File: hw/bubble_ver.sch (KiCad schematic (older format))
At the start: 0 parts

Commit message: - add ic (freescale mkl02), temp sensor (silabs si7020), bubble display (hp qdsp-6040) to schematic
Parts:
- added D?: QDSP-6040, symbol QDSP-6040
- added U?: MKL02ZXVFG4, ~, symbol MKL02ZXVFG4
- added U?: SI7020, ~, symbol SI7020
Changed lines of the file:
@@
 LIBS:contrib
 LIBS:valves
+LIBS:kicadlib
+LIBS:bubble_ver-cache
 EELAYER 27 0
 EELAYER END
@@
 Comment4 ""
 $EndDescr
+$Comp
+L MKL02ZXVFG4 U?
+U 1 1 539905F5
+P 4500 3000
+F 0 "U?" H 4050 2400 60  0000 C CNN
+F 1 "MKL02ZXVFG4" H 5200 2400 60  0000 C CNN
+F 2 "~" H 4500 3000 60  0000 C CNN
+F 3 "~" H 4500 3000 60  0000 C CNN
+	1    4500 3000
+	1    0    0    -1
+$EndComp
+$Comp
+L SI7020 U?
+U 1 1 53990604
+P 6250 4500
+F 0 "U?" H 6250 4200 60  0000 C CNN
+F 1 "SI7020" H 6250 4800 60  0000 C CNN
+F 2 "~" H 6250 4400 60  0000 C CNN
+F 3 "~" H 6250 4400 60  0000 C CNN
+	1    6250 4500
+	1    0    0    -1
+$EndComp
+$Comp
+L QDSP-6040 D?
+U 1 1 5399119B
+P 7700 3900
+F 0 "D?" H 8600 4650 60  0000 C CNN
+F 1 "QDSP-6040" V 7550 4650 60  0000 C CNN
+F 2 "" H 8500 4400 60  0000 C CNN
+F 3 "" H 8500 4400 60  0000 C CNN
+	1    7700 3900
+	1    0    0    -1
+$EndComp
 $EndSCHEMATC

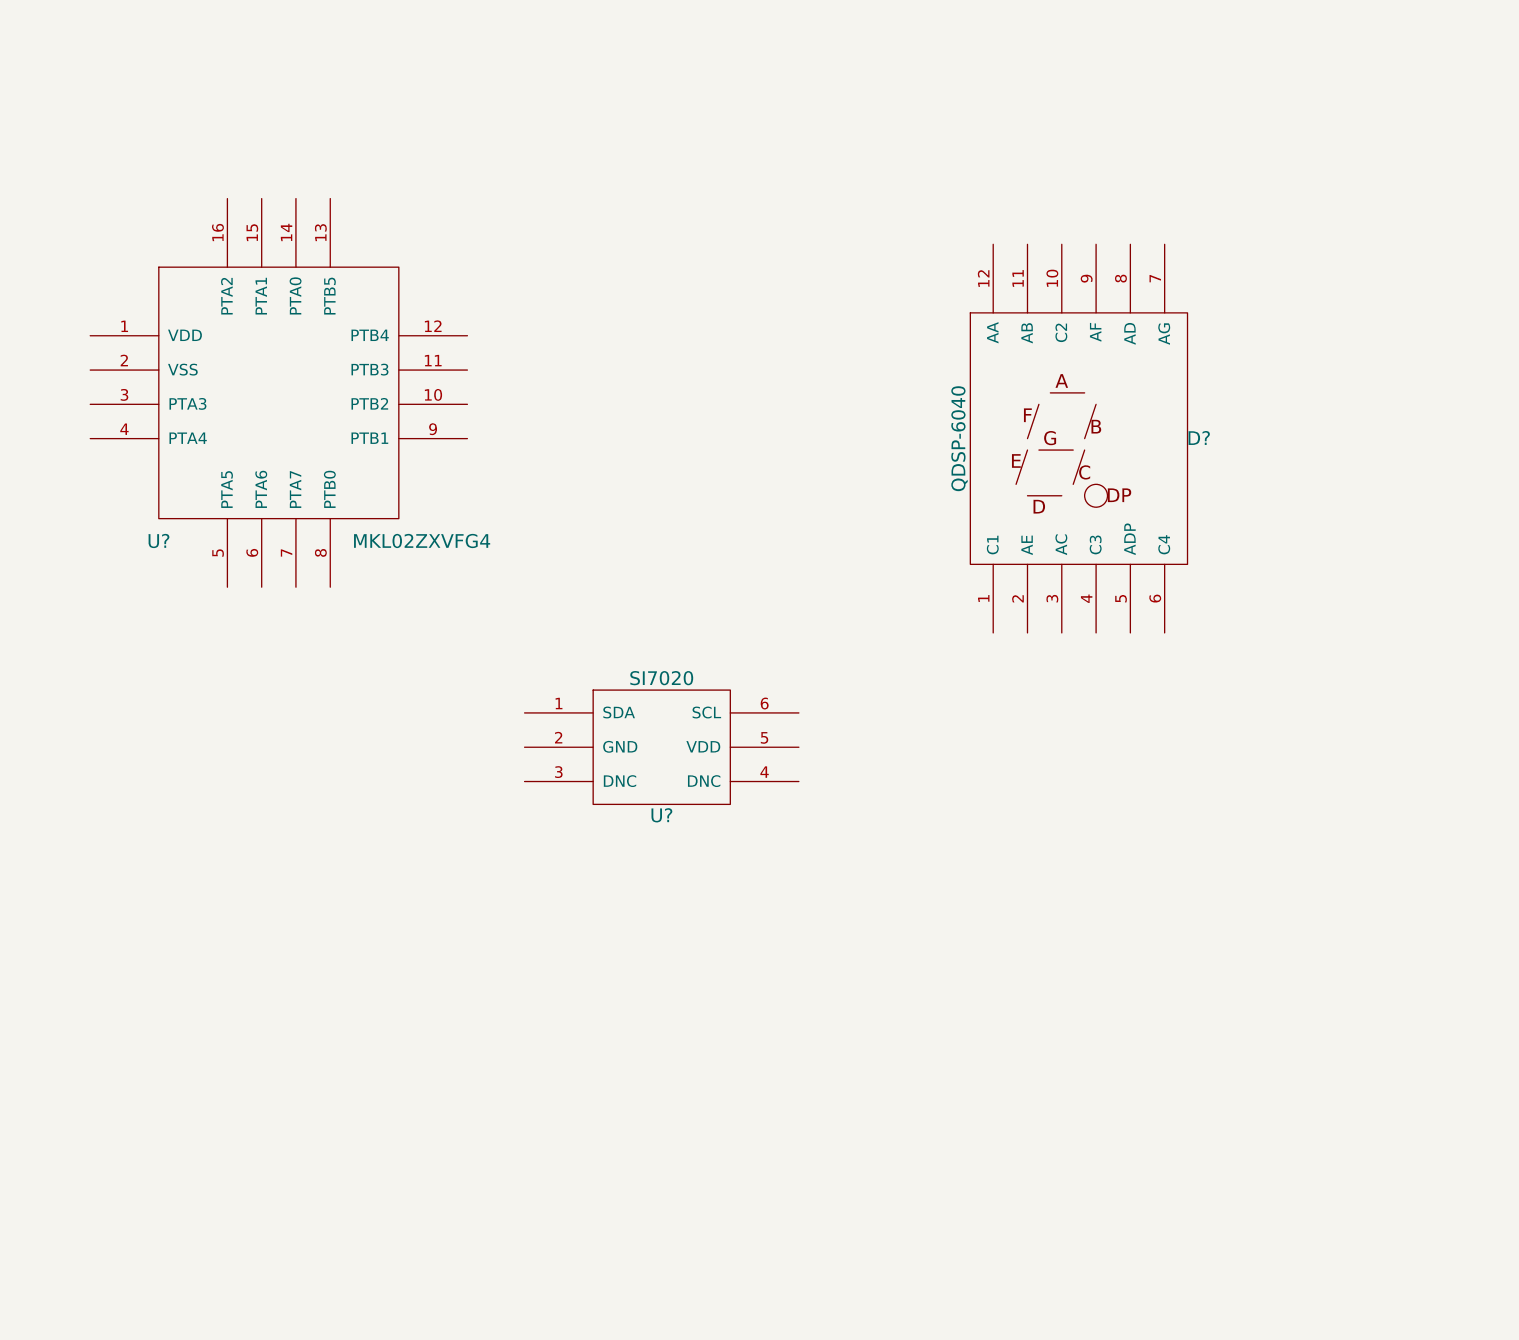
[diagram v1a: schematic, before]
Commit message: - start flushing out schematic. use dual-io multiplexing for leds (better than charlieplexing, no leak, and I have enough MCU pins)
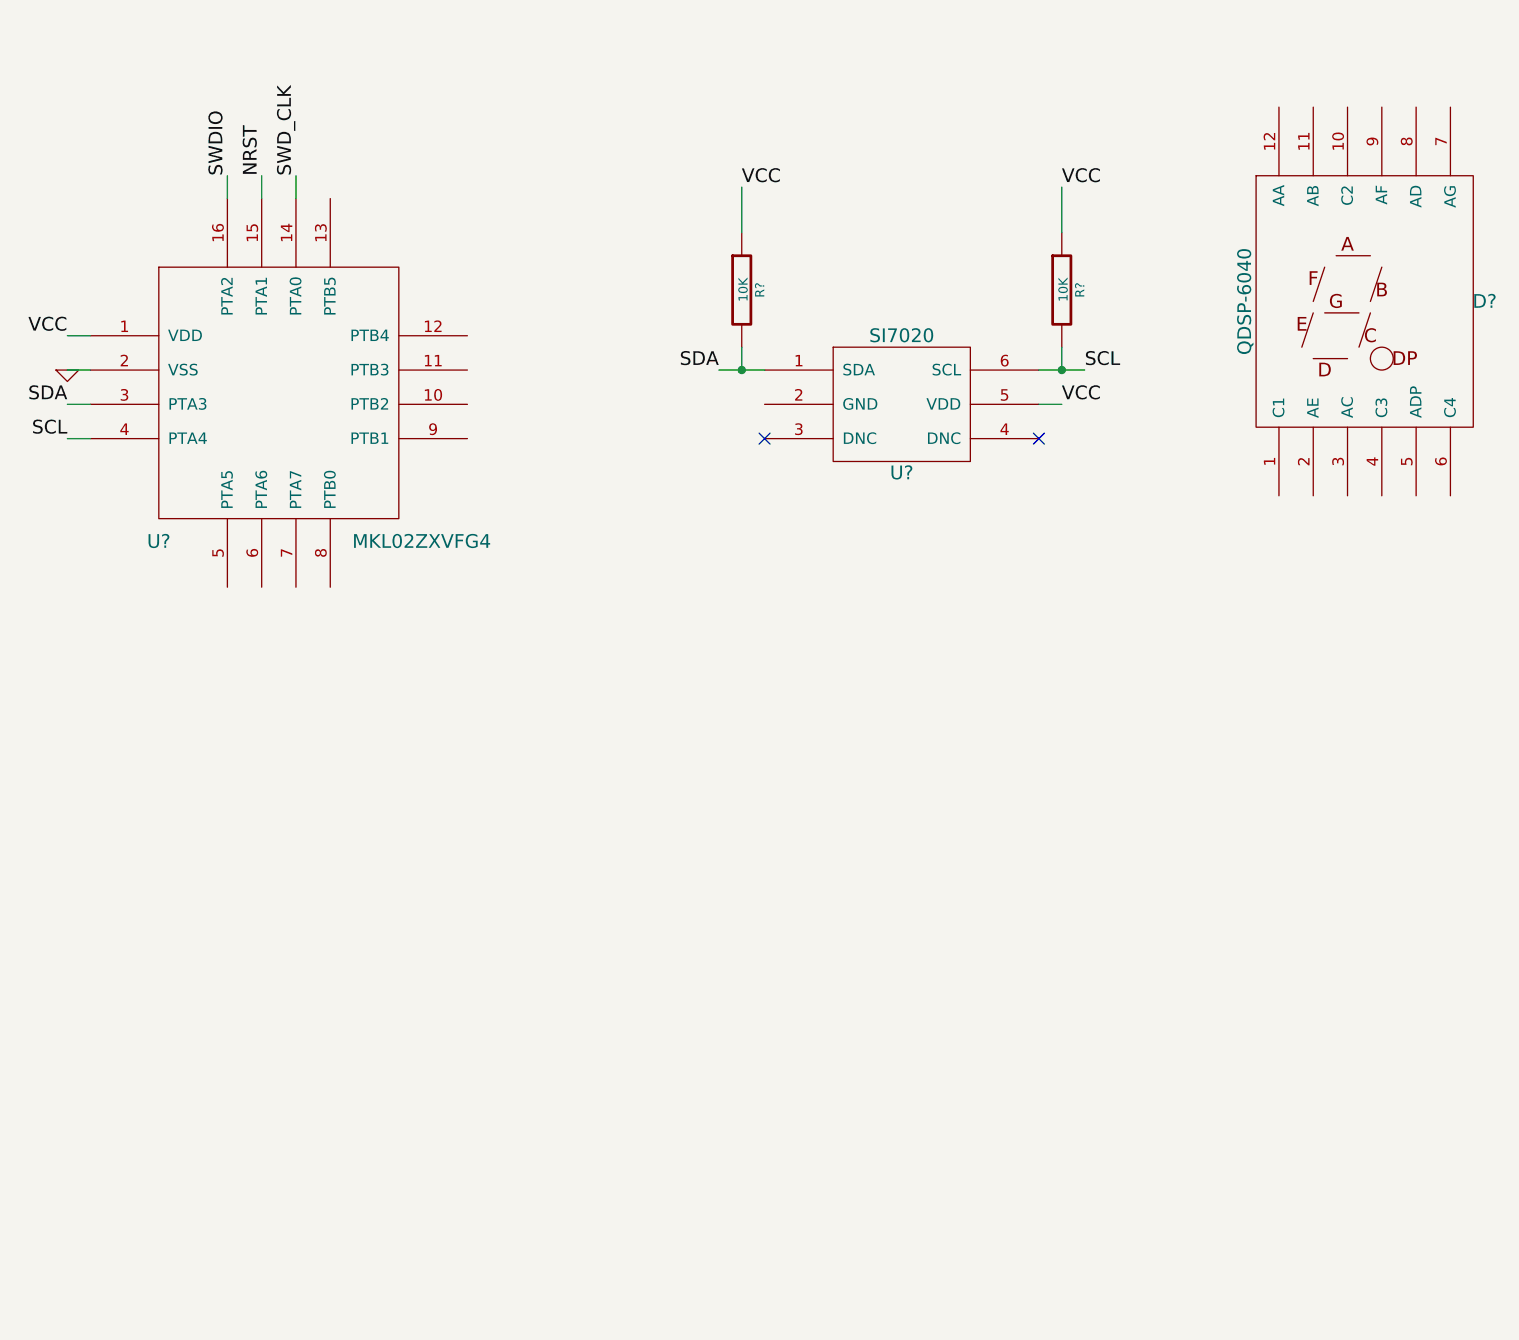
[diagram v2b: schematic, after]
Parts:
- added R? (x2): 10K, ~, symbol R
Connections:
- net VCC: now reaches U?.1 (VDD)
- net VCC: now also U?.5 (VDD), R?.1, R?.1
- net SWD_CLK: now reaches U?.14 (PTA0)
- net NRST: now reaches U?.15 (PTA1)
- net SWDIO: now reaches U?.16 (PTA2)
- net GND: now reaches U?.2 (VSS)
- net SDA: now reaches U?.3 (PTA3)
- net SDA: now also U?.1 (SDA), R?.2
- net SCL: now reaches U?.4 (PTA4)
- net SCL: now also U?.6 (SCL), R?.2
- no-connect marks 0 -> 2
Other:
- moved on the sheet: D?, U?
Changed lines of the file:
@@
 L SI7020 U?
 U 1 1 53990604
-P 6250 4500
-F 0 "U?" H 6250 4200 60  0000 C CNN
-F 1 "SI7020" H 6250 4800 60  0000 C CNN
-F 2 "~" H 6250 4400 60  0000 C CNN
-F 3 "~" H 6250 4400 60  0000 C CNN
-	1    6250 4500
+P 7300 3000
+F 0 "U?" H 7300 2700 60  0000 C CNN
+F 1 "SI7020" H 7300 3300 60  0000 C CNN
+F 2 "~" H 7300 2900 60  0000 C CNN
+F 3 "~" H 7300 2900 60  0000 C CNN
+	1    7300 3000
 	1    0    0    -1
 $EndComp
@@
 L QDSP-6040 D?
 U 1 1 5399119B
-P 7700 3900
-F 0 "D?" H 8600 4650 60  0000 C CNN
-F 1 "QDSP-6040" V 7550 4650 60  0000 C CNN
-F 2 "" H 8500 4400 60  0000 C CNN
-F 3 "" H 8500 4400 60  0000 C CNN
-	1    7700 3900
+P 8950 3300
+F 0 "D?" H 9850 4050 60  0000 C CNN
+F 1 "QDSP-6040" V 8800 4050 60  0000 C CNN
+F 2 "" H 9750 3800 60  0000 C CNN
+F 3 "" H 9750 3800 60  0000 C CNN
+	1    8950 3300
 	1    0    0    -1
 $EndComp
+$Comp
+L R R?
+U 1 1 5399E115
+P 6600 2500
+F 0 "R?" V 6680 2500 40  0000 C CNN
+F 1 "10K" V 6607 2501 40  0000 C CNN
+F 2 "~" V 6530 2500 30  0000 C CNN
+F 3 "~" H 6600 2500 30  0000 C CNN
+	1    6600 2500
+	1    0    0    -1
+$EndComp
+$Comp
+L R R?
+U 1 1 5399E127
+P 8000 2500
+F 0 "R?" V 8080 2500 40  0000 C CNN
+F 1 "10K" V 8007 2501 40  0000 C CNN
+F 2 "~" V 7930 2500 30  0000 C CNN
+F 3 "~" H 8000 2500 30  0000 C CNN
+	1    8000 2500
+	1    0    0    -1
+$EndComp
+Wire Wire Line
+	6600 2250 6600 2050
+Wire Wire Line
+	8000 2250 8000 2050
+Text Label 8000 2050 0    60   ~ 0
+VCC
+Text Label 6600 2050 0    60   ~ 0
+VCC
+Wire Wire Line
+	8000 2750 8000 2850
+Wire Wire Line
+	7900 2850 8100 2850
+Wire Wire Line
+	6500 2850 6700 2850
+Wire Wire Line
+	6600 2850 6600 2750
+NoConn ~ 7900 3150
+NoConn ~ 6700 3150
+Connection ~ 8000 2850
+Connection ~ 6600 2850
+Text Label 8100 2850 0    60   ~ 0
+SCL
+Text Label 6500 2850 2    60   ~ 0
+SDA
+Text Label 3650 3000 2    60   ~ 0
+SDA
+Text Label 3650 3150 2    60   ~ 0
+SCL
+Wire Wire Line
+	3750 3000 3650 3000
+Wire Wire Line
+	3650 3150 3750 3150
+Text Label 3650 2700 2    60   ~ 0
+VCC
+Wire Wire Line
+	3650 2700 3750 2700
+$Comp
+L GND #PWR?
+U 1 1 5399E2DF
+P 3650 2850
+F 0 "#PWR?" H 3650 2850 30  0001 C CNN
+F 1 "GND" H 3650 2780 30  0001 C CNN
+F 2 "" H 3650 2850 60  0000 C CNN
+F 3 "" H 3650 2850 60  0000 C CNN
+	1    3650 2850
+	1    0    0    -1
+$EndComp
+Wire Wire Line
+	3650 2850 3750 2850
+Text Label 4350 2000 1    60   ~ 0
+SWDIO
+Text Label 4500 2000 1    60   ~ 0
+NRST
+Text Label 4650 2000 1    60   ~ 0
+SWD_CLK
+Wire Wire Line
+	4350 2000 4350 2100
+Wire Wire Line
+	4500 2000 4500 2100
+Wire Wire Line
+	4650 2000 4650 2100
+Text Label 8000 3000 0    60   ~ 0
+VCC
+Wire Wire Line
+	8000 3000 7900 3000
 $EndSCHEMATC

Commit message: - add resistor networks and most net names.
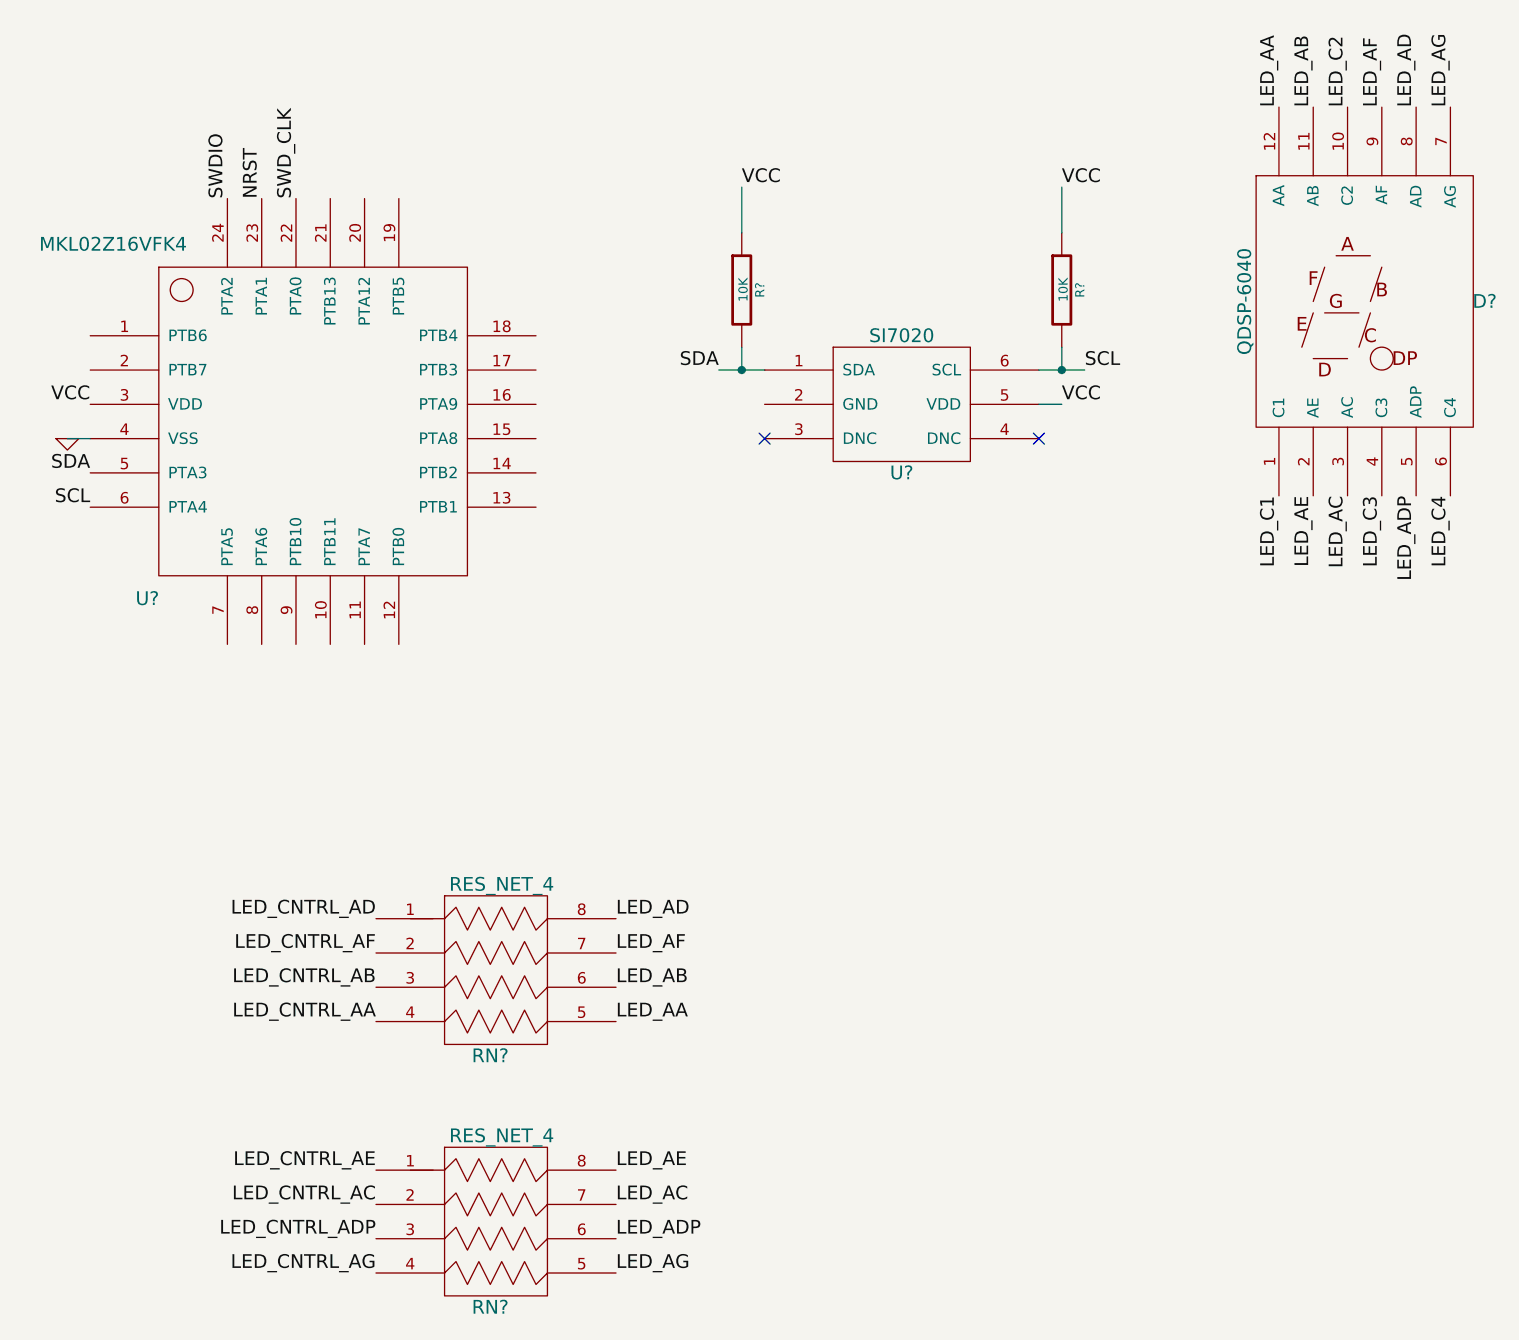
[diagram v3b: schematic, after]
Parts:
- removed U?: MKL02ZXVFG4, ~, symbol MKL02ZXVFG4
- added RN? (x2): RES_NET_4, symbol RES_NET_4
- added U?: MKL02Z16VFK4, symbol MKL02Z16VFK4
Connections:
- net GND: now also U?.4 (VSS)
- net NRST: now also U?.23 (PTA1)
- net SCL: now also U?.6 (PTA4)
- net SDA: now also U?.5 (PTA3)
- net SWDIO: now also U?.24 (PTA2)
- net SWD_CLK: now also U?.22 (PTA0)
- net VCC: now also U?.3 (VDD)
- net LED_C1: now reaches D?.1 (C1)
- net LED_C2: now reaches D?.10 (C2)
- net LED_AB: now reaches D?.11 (AB)
- net LED_AB: now also RN?.6
- net LED_AA: now reaches D?.12 (AA)
- net LED_AA: now also RN?.5
- net LED_AE: now reaches D?.2 (AE)
- net LED_AE: now also RN?.8
- net LED_AC: now reaches D?.3 (AC)
- net LED_AC: now also RN?.7
- net LED_C3: now reaches D?.4 (C3)
- net LED_ADP: now reaches D?.5 (ADP)
- net LED_ADP: now also RN?.6
- net LED_C4: now reaches D?.6 (C4)
- net LED_AG: now reaches D?.7 (AG)
- net LED_AG: now also RN?.5
- net LED_AD: now reaches D?.8 (AD)
- net LED_AD: now also RN?.8
- net LED_AF: now reaches D?.9 (AF)
- net LED_AF: now also RN?.7
- new net LED_CNTRL_AA: RN?.4
- new net LED_CNTRL_AB: RN?.3
- new net LED_CNTRL_AC: RN?.2
- new net LED_CNTRL_AD: RN?.1
- new net LED_CNTRL_ADP: RN?.3
- new net LED_CNTRL_AE: RN?.1
- new net LED_CNTRL_AF: RN?.2
- new net LED_CNTRL_AG: RN?.4
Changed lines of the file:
@@
 $EndDescr
-$Comp
-L MKL02ZXVFG4 U?
-U 1 1 539905F5
-P 4500 3000
-F 0 "U?" H 4050 2400 60  0000 C CNN
-F 1 "MKL02ZXVFG4" H 5200 2400 60  0000 C CNN
-F 2 "~" H 4500 3000 60  0000 C CNN
-F 3 "~" H 4500 3000 60  0000 C CNN
-	1    4500 3000
-	1    0    0    -1
-$EndComp
 $Comp
 L SI7020 U?
@@
 Text Label 6500 2850 2    60   ~ 0
 SDA
-Text Label 3650 3000 2    60   ~ 0
+Text Label 3750 3300 2    60   ~ 0
 SDA
-Text Label 3650 3150 2    60   ~ 0
+Text Label 3750 3450 2    60   ~ 0
 SCL
-Wire Wire Line
-	3750 3000 3650 3000
-Wire Wire Line
-	3650 3150 3750 3150
-Text Label 3650 2700 2    60   ~ 0
+Text Label 3750 3000 2    60   ~ 0
 VCC
-Wire Wire Line
-	3650 2700 3750 2700
 $Comp
 L GND #PWR?
 U 1 1 5399E2DF
-P 3650 2850
-F 0 "#PWR?" H 3650 2850 30  0001 C CNN
-F 1 "GND" H 3650 2780 30  0001 C CNN
-F 2 "" H 3650 2850 60  0000 C CNN
-F 3 "" H 3650 2850 60  0000 C CNN
-	1    3650 2850
+P 3650 3150
+F 0 "#PWR?" H 3650 3150 30  0001 C CNN
+F 1 "GND" H 3650 3080 30  0001 C CNN
+F 2 "" H 3650 3150 60  0000 C CNN
+F 3 "" H 3650 3150 60  0000 C CNN
+	1    3650 3150
 	1    0    0    -1
 $EndComp
 Wire Wire Line
-	3650 2850 3750 2850
-Text Label 4350 2000 1    60   ~ 0
+	3650 3150 3750 3150
+Text Label 4350 2100 1    60   ~ 0
 SWDIO
-Text Label 4500 2000 1    60   ~ 0
+Text Label 4500 2100 1    60   ~ 0
 NRST
-Text Label 4650 2000 1    60   ~ 0
+Text Label 4650 2100 1    60   ~ 0
 SWD_CLK
-Wire Wire Line
-	4350 2000 4350 2100
-Wire Wire Line
-	4500 2000 4500 2100
-Wire Wire Line
-	4650 2000 4650 2100
 Text Label 8000 3000 0    60   ~ 0
 VCC
 Wire Wire Line
 	8000 3000 7900 3000
+Text Label 8950 1700 1    60   ~ 0
+LED_AA
+Text Label 9100 1700 1    60   ~ 0
+LED_AB
+Text Label 9100 3400 3    60   ~ 0
+LED_AE
+Text Label 9250 3400 3    60   ~ 0
+LED_AC
+$Comp
+L MKL02Z16VFK4 U?
+U 1 1 5399EECC
+P 4500 3150
+F 0 "U?" H 4000 2450 60  0000 C CNN
+F 1 "MKL02Z16VFK4" H 3850 4000 60  0000 C CNN
+F 2 "" H 4500 3150 60  0000 C CNN
+F 3 "" H 4500 3150 60  0000 C CNN
+	1    4500 3150
+	1    0    0    -1
+$EndComp
+Text Label 9250 1700 1    60   ~ 0
+LED_C2
+Text Label 9400 1700 1    60   ~ 0
+LED_AF
+Text Label 9550 1700 1    60   ~ 0
+LED_AD
+Text Label 9700 1700 1    60   ~ 0
+LED_AG
+Text Label 8950 3400 3    60   ~ 0
+LED_C1
+Text Label 9400 3400 3    60   ~ 0
+LED_C3
+Text Label 9550 3400 3    60   ~ 0
+LED_ADP
+Text Label 9700 3400 3    60   ~ 0
+LED_C4
+Text Label 6050 6350 0    60   ~ 0
+LED_AE
+Text Label 6050 6500 0    60   ~ 0
+LED_AC
+Text Label 6050 6650 0    60   ~ 0
+LED_ADP
+Text Label 6050 5700 0    60   ~ 0
+LED_AA
+Text Label 6050 5550 0    60   ~ 0
+LED_AB
+Text Label 6050 5400 0    60   ~ 0
+LED_AF
+Text Label 6050 5250 0    60   ~ 0
+LED_AD
+Text Label 6050 6800 0    60   ~ 0
+LED_AG
+Text Label 5000 5700 2    60   ~ 0
+LED_CNTRL_AA
+Text Label 5000 5550 2    60   ~ 0
+LED_CNTRL_AB
+Text Label 5000 5400 2    60   ~ 0
+LED_CNTRL_AF
+Text Label 5000 5250 2    60   ~ 0
+LED_CNTRL_AD
+Text Label 5000 6800 2    60   ~ 0
+LED_CNTRL_AG
+Text Label 5000 6650 2    60   ~ 0
+LED_CNTRL_ADP
+Text Label 5000 6500 2    60   ~ 0
+LED_CNTRL_AC
+Text Label 5000 6350 2    60   ~ 0
+LED_CNTRL_AE
+$Comp
+L RES_NET_4 RN?
+U 1 1 5399F32C
+P 5600 5550
+F 0 "RN?" H 5500 5250 60  0000 C CNN
+F 1 "RES_NET_4" H 5550 6000 60  0000 C CNN
+F 2 "" H 5250 5450 60  0000 C CNN
+F 3 "" H 5250 5450 60  0000 C CNN
+	1    5600 5550
+	1    0    0    -1
+$EndComp
+$Comp
+L RES_NET_4 RN?
+U 1 1 5399F343
+P 5600 6650
+F 0 "RN?" H 5500 6350 60  0000 C CNN
+F 1 "RES_NET_4" H 5550 7100 60  0000 C CNN
+F 2 "" H 5250 6550 60  0000 C CNN
+F 3 "" H 5250 6550 60  0000 C CNN
+	1    5600 6650
+	1    0    0    -1
+$EndComp
 $EndSCHEMATC
